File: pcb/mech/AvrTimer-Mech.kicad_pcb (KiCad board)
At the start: 2 copper layers, 62.9 x 49.4 mm, 28 parts, among them J1 USB_B_Micro, Q1 BC846, SW1 SW_DIP_x01, SW2 SW_DIP_x01, SW3 SW_DIP_x01, SW4 SW_DPDT_x2, SW5 SW_DIP_x02, U1 L7805

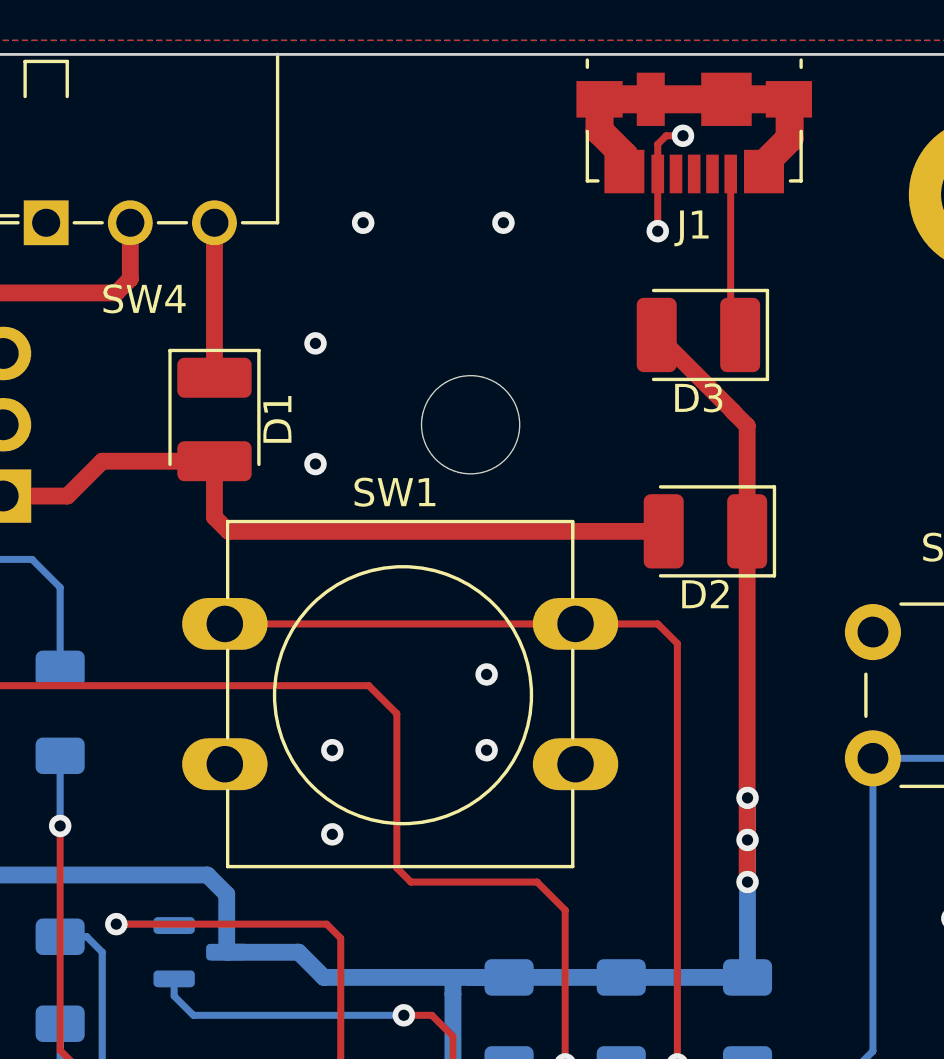
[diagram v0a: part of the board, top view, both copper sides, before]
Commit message: Replace diode footprints to shop real ones
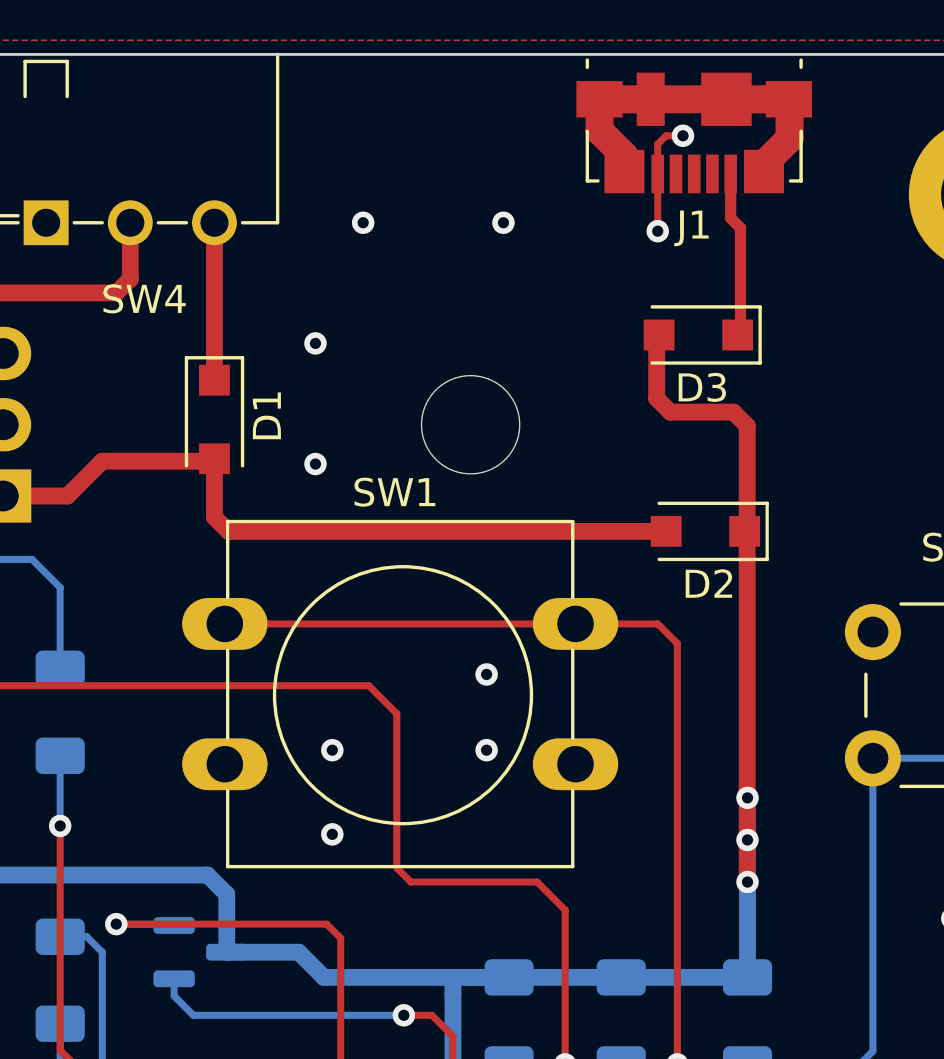
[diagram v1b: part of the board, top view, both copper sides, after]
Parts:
- D1, D2, D3: footprint Diode_SMD:D_1210_3225Metric_Pad1.42x2.65mm_HandSolder -> Diode_SMD:D_SOD-123F
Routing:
- net VCC: track 121.2 -> 122.5 mm

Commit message: Update after Alexander's review
Change-Id: Ia4ad441f5e963f780b6a0a3a3c0dc55fa8eb64d7
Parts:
- added C5: C, Capacitor_SMD:C_0402_1005Metric_Pad0.74x0.62mm_HandSolder, F.Cu at (144.5, 69.1)
- added C6: C, Capacitor_SMD:C_0402_1005Metric_Pad0.74x0.62mm_HandSolder, F.Cu at (147.5, 69.1)
- added R6: R, Resistor_SMD:R_1206_3216Metric_Pad1.30x1.75mm_HandSolder, F.Cu at (140.5, 69.0)
- moved U1 42.8 mm to (149.5, 76.2), turned to 0 degrees
- moved ? 12.8 mm to (154.8, 60.0)
- moved ? 12.8 mm to (154.8, 101.5)
- moved ? 1.41 mm to (87.0, 60.0)
- moved ? 1.12 mm to (87.0, 101.5)
- moved D3 0.25 mm to (131.5, 66.0)
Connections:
- J1 pad 6: unconnected-(J1-Pad6) -> Net-(J1-Pad6)
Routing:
- net Net-(J1-Pad6): track 0.00 -> 32.4 mm
- net Net-(C1-Pad1): track 70.3 -> 99.8 mm, vias 3 -> 6
- net unconnected-(J1-Pad6): track 12.7 -> 0.00 mm
- net VCC: track 122.5 -> 119.5 mm
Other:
- board size 62.9 x 49.4 mm -> 75.8 x 49.5 mm

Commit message: [PCB] Add values for R and C
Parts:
- C1: value C_Polarized -> 470 uF
- C2, C3, C5: value C -> 100 nF
- C4: value C_Polarized -> 10 uF
- C6: value C -> 1 nF
- R1, R2, R3: value R -> 10 kOhm
- R4: value R -> 100 Ohm
- R5: value R -> 10 Ohm
- R6: value R -> 1 MOhm
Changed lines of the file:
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@@
   (net 8 "+9V")
   (net 9 "Net-(C1-Pad1)")
-  (net 10 "Net-(J1-Pad6)")
+  (net 10 "Net-(C5-Pad2)")
   (net 11 "unconnected-(J1-Pad4)")
   (net 12 "unconnected-(J1-Pad3)")
@@
       (effects (font (size 1 1) (thickness 0.15)))
     )
-    (fp_text value "R" (at 0 1.82 90) (layer "F.Fab")
+    (fp_text value "1 MOhm" (at 0 1.82 90) (layer "F.Fab")
       (effects (font (size 1 1) (thickness 0.15)))
     )
@@
       (net 2 "GND") (pintype "passive"))
     (pad "2" smd roundrect locked (at 1.55 0 90) (size 1.3 1.75) (layers "F.Cu" "F.Paste" "F.Mask") (roundrect_rratio 0.192308)
-      (net 10 "Net-(J1-Pad6)") (pintype "passive"))
+      (net 10 "Net-(C5-Pad2)") (pintype "passive"))
     (model "${KICAD6_3DMODEL_DIR}/Resistor_SMD.3dshapes/R_1206_3216Metric.wrl"
       (offset (xyz 0 0 0))
@@
       (net 2 "GND") (pinfunction "GND") (pintype "power_out"))
     (pad "6" smd rect locked (at -1.15 1.2 180) (size 1.8 1.9) (layers "F.Cu" "F.Paste" "F.Mask")
-      (net 10 "Net-(J1-Pad6)") (pinfunction "Shield") (pintype "passive"))
+      (net 10 "Net-(C5-Pad2)") (pinfunction "Shield") (pintype "passive"))
     (pad "6" smd rect locked (at -2.4875 -1.375 180) (size 1.425 1.55) (layers "F.Cu" "F.Paste" "F.Mask")
-      (net 10 "Net-(J1-Pad6)") (pinfunction "Shield") (pintype "passive"))
+      (net 10 "Net-(C5-Pad2)") (pinfunction "Shield") (pintype "passive"))
     (pad "6" smd rect locked (at 1.55 1.2 180) (size 1 1.9) (layers "F.Cu" "F.Paste" "F.Mask")
-      (net 10 "Net-(J1-Pad6)") (pinfunction "Shield") (pintype "passive"))
+      (net 10 "Net-(C5-Pad2)") (pinfunction "Shield") (pintype "passive"))
     (pad "6" smd rect locked (at 3.375 1.2 180) (size 1.65 1.3) (layers "F.Cu" "F.Paste" "F.Mask")
-      (net 10 "Net-(J1-Pad6)") (pinfunction "Shield") (pintype "passive"))
+      (net 10 "Net-(C5-Pad2)") (pinfunction "Shield") (pintype "passive"))
     (pad "6" smd rect locked (at 2.4875 -1.375 180) (size 1.425 1.55) (layers "F.Cu" "F.Paste" "F.Mask")
-      (net 10 "Net-(J1-Pad6)") (pinfunction "Shield") (pintype "passive"))
+      (net 10 "Net-(C5-Pad2)") (pinfunction "Shield") (pintype "passive"))
     (pad "6" smd rect locked (at -3.375 1.2 180) (size 1.65 1.3) (layers "F.Cu" "F.Paste" "F.Mask")
-      (net 10 "Net-(J1-Pad6)") (pinfunction "Shield") (pintype "passive"))
+      (net 10 "Net-(C5-Pad2)") (pinfunction "Shield") (pintype "passive"))
     (model "${KICAD6_3DMODEL_DIR}/Connector_USB.3dshapes/USB_Micro-B_Molex_47346-0001.wrl"
       (offset (xyz 0 0 0))
@@
       (effects (font (size 1 1) (thickness 0.15)))
     )
-    (fp_text value "C" (at 0 1.16 90) (layer "F.Fab")
+    (fp_text value "1 nF" (at 0 1.16 90) (layer "F.Fab")
       (effects (font (size 1 1) (thickness 0.15)))
     )
@@
       (net 2 "GND") (pintype "passive"))
     (pad "2" smd roundrect locked (at 0.5675 0 90) (size 0.735 0.62) (layers "F.Cu" "F.Paste" "F.Mask") (roundrect_rratio 0.25)
-      (net 10 "Net-(J1-Pad6)") (pintype "passive"))
+      (net 10 "Net-(C5-Pad2)") (pintype "passive"))
     (model "${KICAD6_3DMODEL_DIR}/Capacitor_SMD.3dshapes/C_0402_1005Metric.wrl"
       (offset (xyz 0 0 0))
@@
     (property "Sheetname" "")
     (attr smd)
-    (fp_text reference "D3" (at -0.127 -1.905 180) (layer "F.SilkS")
-      (effects (font (size 1 1) (thickness 0.15)))
-    )
-    (fp_text value "DIODE" (at 0 2.1 180) (layer "F.Fab")
-      (effects (font (size 1 1) (thickness 0.15)))
-    )
-    (fp_text user "${REFERENCE}" (at -0.127 -1.905 180) (layer "F.Fab")
+    (fp_text reference "D3" (at -0.127 -1.905) (layer "F.SilkS")
+      (effects (font (size 1 1) (thickness 0.15)))
+    )
+    (fp_text value "DIODE" (at 0 2.1) (layer "F.Fab")
+      (effects (font (size 1 1) (thickness 0.15)))
+    )
+    (fp_text user "${REFERENCE}" (at -0.127 -1.905) (layer "F.Fab")
       (effects (font (size 1 1) (thickness 0.15)))
     )
@@
     (fp_line (start 1.4 0.9) (end -1.4 0.9) (layer "F.Fab") (width 0.1))
     (pad "1" smd rect locked (at -1.4 0 180) (size 1.1 1.1) (layers "F.Cu" "F.Paste" "F.Mask")
-      (net 15 "Net-(D3-Pad1)") (pinfunction "K") (pintype "input"))
+      (net 15 "Net-(D3-Pad1)") (pinfunction "K"))
     (pad "2" smd rect locked (at 1.4 0 180) (size 1.1 1.1) (layers "F.Cu" "F.Paste" "F.Mask")
-      (net 3 "VCC") (pinfunction "A") (pintype "input"))
+      (net 3 "VCC") (pinfunction "A"))
     (model "${KICAD6_3DMODEL_DIR}/Diode_SMD.3dshapes/D_SOD-123F.wrl"
       (offset (xyz 0 0 0))
@@
       (effects (font (size 1 1) (thickness 0.15)))
     )
-    (fp_text value "C" (at 0 1.16 90) (layer "F.Fab")
+    (fp_text value "100 nF" (at 0 1.16 90) (layer "F.Fab")
       (effects (font (size 1 1) (thickness 0.15)))
     )
@@
       (net 2 "GND") (pintype "passive"))
     (pad "2" smd roundrect locked (at 0.5675 0 90) (size 0.735 0.62) (layers "F.Cu" "F.Paste" "F.Mask") (roundrect_rratio 0.25)
-      (net 10 "Net-(J1-Pad6)") (pintype "passive"))
+      (net 10 "Net-(C5-Pad2)") (pintype "passive"))
     (model "${KICAD6_3DMODEL_DIR}/Capacitor_SMD.3dshapes/C_0402_1005Metric.wrl"
       (offset (xyz 0 0 0))
@@
       (effects (font (size 1 1) (thickness 0.15)))
     )
-    (fp_text value "C_Polarized" (at 2.5 6.25) (layer "F.Fab")
+    (fp_text value "470 uF" (at 2.5 6.25) (layer "F.Fab")
       (effects (font (size 1 1) (thickness 0.15)))
     )
@@
       (effects (font (size 1 1) (thickness 0.15)))
     )
-    (fp_text value "C_Polarized" (at 2.5 6.25) (layer "F.Fab")
+    (fp_text value "10 uF" (at 2.5 6.25) (layer "F.Fab")
       (effects (font (size 1 1) (thickness 0.15)))
     )
@@
       (effects (font (size 1 1) (thickness 0.15)) (justify mirror))
     )
-    (fp_text value "C" (at 0 -1.16) (layer "B.Fab")
+    (fp_text value "100 nF" (at 0 -1.16) (layer "B.Fab")
       (effects (font (size 1 1) (thickness 0.15)) (justify mirror))
     )
@@
       (effects (font (size 1 1) (thickness 0.15)) (justify mirror))
     )
-    (fp_text value "R" (at 0 -1.82 90) (layer "B.Fab")
+    (fp_text value "100 Ohm" (at 0 -1.82 90) (layer "B.Fab")
       (effects (font (size 1 1) (thickness 0.15)) (justify mirror))
     )
@@
       (effects (font (size 1 1) (thickness 0.15)) (justify mirror))
     )
-    (fp_text value "R" (at 0 -1.82 90) (layer "B.Fab")
+    (fp_text value "10 kOhm" (at 0 -1.82 90) (layer "B.Fab")
       (effects (font (size 1 1) (thickness 0.15)) (justify mirror))
     )
@@
       (effects (font (size 1 1) (thickness 0.15)) (justify mirror))
     )
-    (fp_text value "C" (at 0 -1.16) (layer "B.Fab")
+    (fp_text value "100 nF" (at 0 -1.16) (layer "B.Fab")
       (effects (font (size 1 1) (thickness 0.15)) (justify mirror))
     )
@@
       (effects (font (size 1 1) (thickness 0.15)) (justify mirror))
     )
-    (fp_text value "R" (at 0 -1.82 90) (layer "B.Fab")
+    (fp_text value "10 Ohm" (at 0 -1.82 90) (layer "B.Fab")
       (effects (font (size 1 1) (thickness 0.15)) (justify mirror))
     )
@@
       (effects (font (size 1 1) (thickness 0.15)) (justify mirror))
     )
-    (fp_text value "R" (at 0 -1.82 90) (layer "B.Fab")
+    (fp_text value "10 kOhm" (at 0 -1.82 90) (layer "B.Fab")
       (effects (font (size 1 1) (thickness 0.15)) (justify mirror))
     )
@@
     (pad "" np_thru_hole oval locked (at 2.54 16.66) (size 3.5 3.5) (drill 3.5) (layers *.Cu *.Mask))
     (pad "1" thru_hole rect locked (at 0 0) (size 1.905 2) (drill 1.1) (layers *.Cu *.Mask)
-      (net 9 "Net-(C1-Pad1)") (pinfunction "IN"))
+      (net 9 "Net-(C1-Pad1)") (pinfunction "IN") (pintype "power_in"))
     (pad "2" thru_hole oval locked (at 2.54 0) (size 1.905 2) (drill 1.1) (layers *.Cu *.Mask)
-      (net 2 "GND") (pinfunction "GND"))
+      (net 2 "GND") (pinfunction "GND") (pintype "power_in"))
     (pad "3" thru_hole oval locked (at 5.08 0) (size 1.905 2) (drill 1.1) (layers *.Cu *.Mask)
-      (net 3 "VCC") (pinfunction "OUT"))
+      (net 3 "VCC") (pinfunction "OUT") (pintype "power_out"))
     (model "${KICAD6_3DMODEL_DIR}/Package_TO_SOT_THT.3dshapes/TO-220-3_Horizontal_TabDown.wrl"
       (offset (xyz 0 0 0))
@@
       (effects (font (size 1 1) (thickness 0.15)) (justify mirror))
     )
-    (fp_text value "R" (at 0 -1.82 90) (layer "B.Fab")
-      (effects (font (size 1 1) (thickness 0.15)) (justify mirror))
-    )
+    (fp_text value "10 kOhm" (at 0 -1.82 90) (layer "B.Fab")
+      (effects (font (size 1 1) (thickness 0.15)) (justify mirror))
+    )
